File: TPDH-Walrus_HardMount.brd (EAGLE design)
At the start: 16 x 40 mm, 37 parts, among them Q2 DMG3404, U1 MS5803-14BA, U2 SN65HVD33RHL, U4 MCP3421A3, U5 TPS79733, U6 MAX6070AAUT18, U7 TXS0102DQM

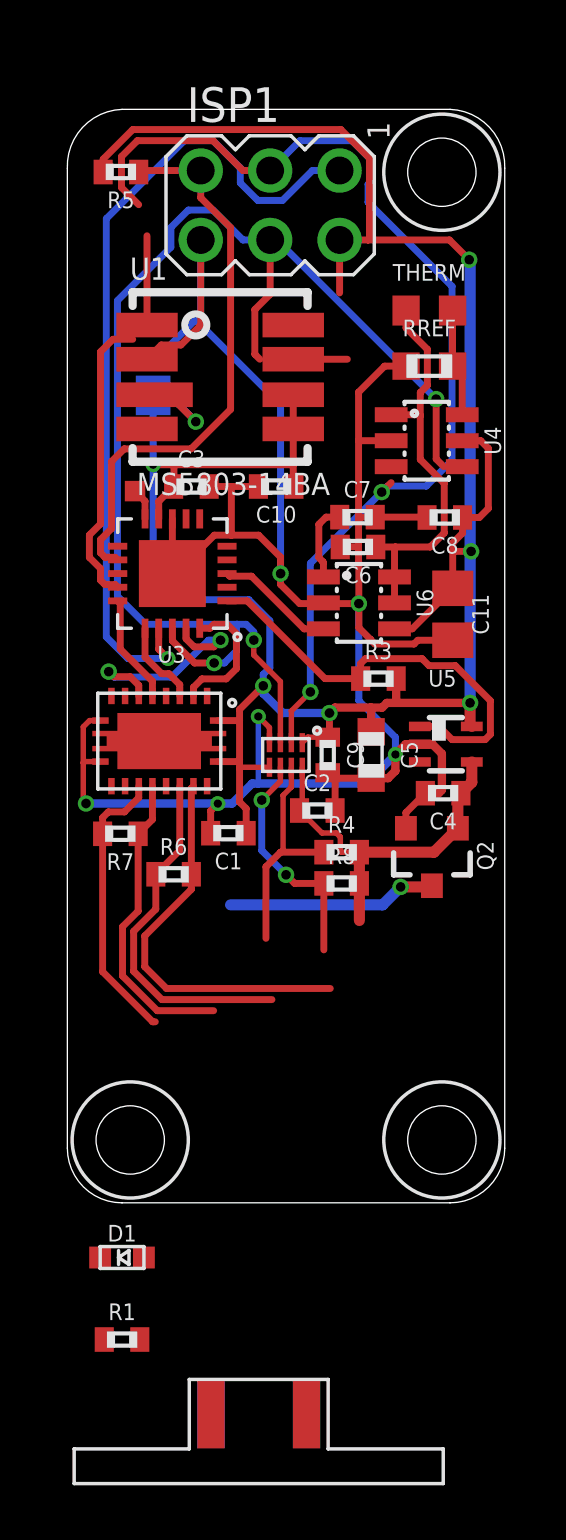
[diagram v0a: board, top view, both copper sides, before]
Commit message: Initial layout for Hard mount (v0.1) variant, cleanup required
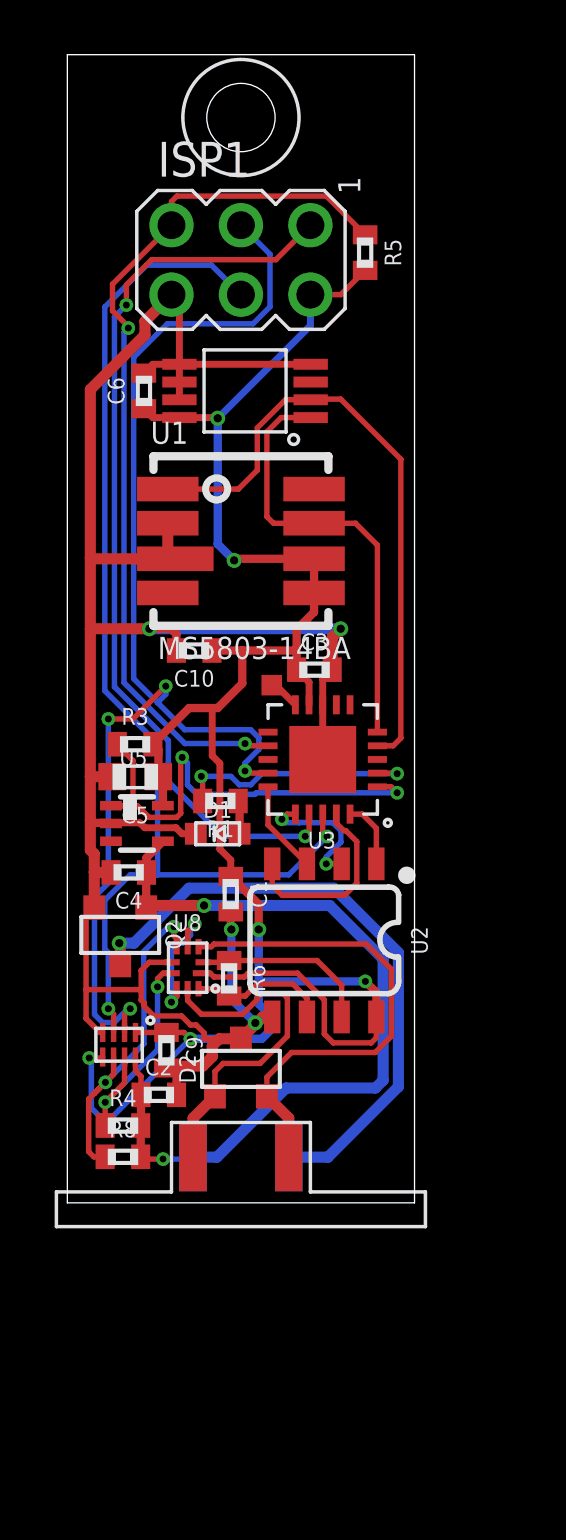
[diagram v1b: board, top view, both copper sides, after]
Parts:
- removed C11: 10uF, bschulz:C0805
- removed C7, C8: 0.1uF, bschulz_passives:C0402
- removed H2, H3: (no value), bschulz:2_56
- removed JP1: JUMPER-SMT_3_1-NC_PASTE_SILK, SparkFun-Jumpers:SMT-JUMPER_3_1-NC_PASTE_SILK
- removed R7: (no value), bschulz_passives:R0402
- removed RREF: 10k, bschulz_passives:R0603
- removed THERM: 10k, bschulz:R0603
- removed U6: MAX6070AAUT18, bschulz:SOT23-6L
- added D2: (no value), bschulz:SOT23-3
- added U8: NS5A4684S, bschulz:WQFN10
- C6: value 0.1uF -> (none)
- U2: value SN65HVD33RHL -> SN65HVD72DSOIC; device bschulz:VQFN-20_POWER -> bschulz:SO08
- U4: value MCP3421A3 -> MCP9808DFNMSOP; device bschulz:SOT23-6L -> bschulz:MSOP_8
- moved R1 20.0 mm to (5.60, 14.7), turned to 180 degrees
- moved D1 15.9 mm to (5.50, 13.5)
- moved R4 12.8 mm to (2.03, 2.83)
- moved R8 12.8 mm to (2.03, 1.68)
- moved C9 12.3 mm to (3.62, 5.58)
- moved U7 12.2 mm to (1.89, 5.78)
- moved C2 11.9 mm to (3.34, 3.95)
- moved C4 11.9 mm to (2.25, 12.1)
- moved Q2 11.8 mm to (1.94, 9.80)
- moved U5 11.7 mm to (2.55, 13.9)
- moved C6 9.69 mm to (2.80, 29.7), turned to 90 degrees
- moved U2 9.47 mm to (9.40, 9.60), turned to 180 degrees
- moved U$1 9.42 mm to (6.35, 0.40)
- moved R5 9.41 mm to (10.9, 34.8), turned to 270 degrees
- moved R3 9.22 mm to (2.48, 16.8)
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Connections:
- removed net N$11: C7.1, U6.1
- removed net SPI-I2C-SWITCH: JP1.2, U1.3
- removed net VREF: C6.1, THERM.1, U4.1, U6.5, U6.6
- removed net VTHERM-: RREF.2, THERM.2, U4.6
- new net OUTPUT_SEL: U8.4, U8.8
- new net TEMP_ALERT: U4.3
- net +3V3: now also C6.1, U2.8, U4.8, U8.1; no longer C11.1, C8.1, JP1.1, U2.1, U2.20, U4.5, U6.4
- net A: now also U2.6, U8.10; no longer R7.2, U2.14, U2.18
- net B: now also U2.7, U8.2; no longer R7.1, U2.15, U2.17
- net GND: now also D2.3, U1.3, U2.5, U4.4, U4.5, U4.6, U4.7, U8.6; no longer C11.2, C7.2, C8.2, JP1.3, RREF.1, U2.10, U2.11, U4.2, U6.2
- net REF_EN: no longer U6.3
- net RX: now also U2.1; no longer U2.3
- net SCL_HV: now also U8.7
- net SCL_OB: now also U4.2; no longer U4.3
- net SDA_HV: now also U8.5
- net SDA_OB: now also U4.1; no longer U4.4
- net SIG1: now also D2.1, U8.9
- net SIG2: now also D2.2, U8.3
- net SN_DE: now also U2.3; no longer U2.6
- net SN_RE: now also U2.2; no longer U2.4
- net TX: now also U2.4; no longer U2.7
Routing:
- net A: track 24.8 -> 5.16 mm
- net SCL_OB: track 3.27 -> 22.9 mm
- net SIG2: track 0.00 -> 18.4 mm
- net +3V3: track 94.0 -> 76.1 mm
- net B: track 24.2 -> 6.63 mm
- net VIN+: track 13.9 -> 30.5 mm, vias 0 -> 2
- net VIN-: track 7.65 -> 22.8 mm
- net VREF: track 14.8 -> 0.00 mm
- net SDA_OB: track 1.98 -> 16.2 mm
- net SIG1: track 0.00 -> 12.8 mm
- net /RESET: track 20.9 -> 32.8 mm, vias 0 -> 2
- net STAT_LED: track 0.00 -> 9.11 mm, vias 0 -> 2
- net GND: track 92.6 -> 84.0 mm, vias 6 -> 4
- net SDA: track 48.7 -> 42.6 mm, vias 3 -> 2
- net OUTPUT_SEL: track 0.00 -> 4.87 mm, vias 0 -> 2
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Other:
- board size 16 x 40 mm -> 12.7 x 42 mm
- board text removed: "I2C <3 m"
- board text removed: "Rx+"
- board text removed: "Rx-"
- board text removed: "SCL"
- board text removed: "SDA"
- board text removed: "Tx+"
- board text removed: "Tx-"
- board text removed: "V+"
- board text removed: "V-"

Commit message: Continued layout, final cleanup required
Cleanup and pours required
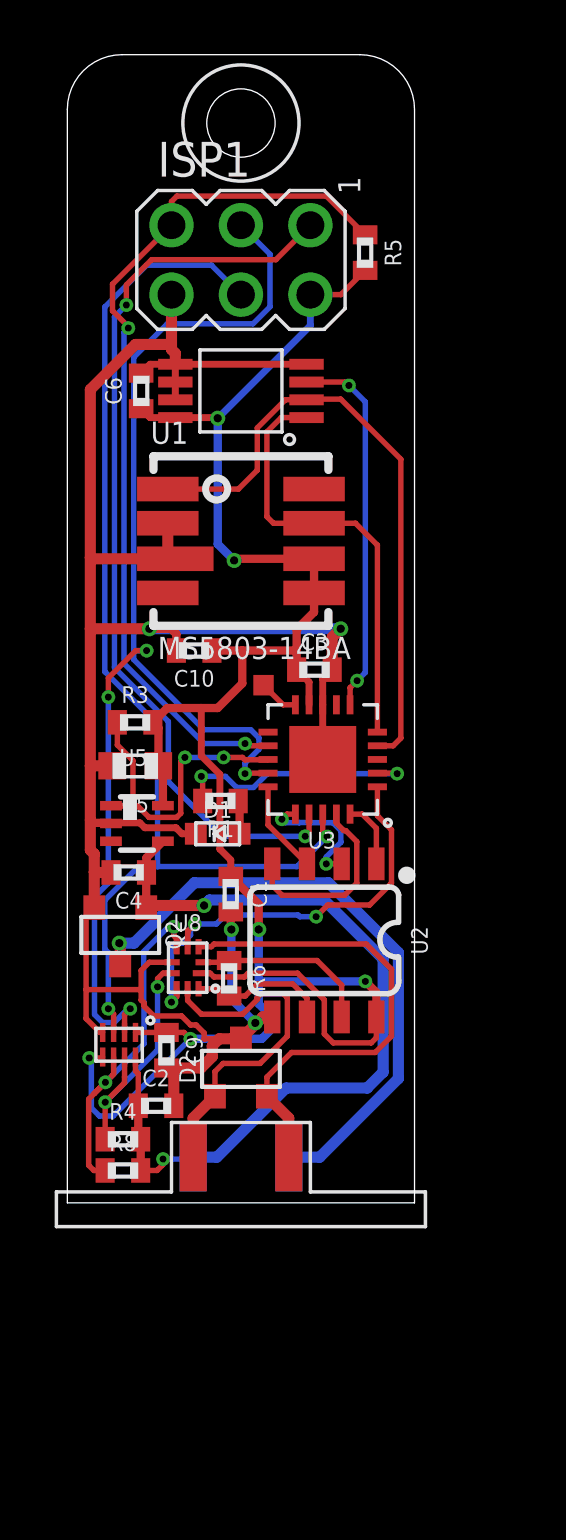
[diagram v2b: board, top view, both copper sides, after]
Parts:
- moved R3 0.80 mm to (2.48, 17.6)
- moved R4 0.50 mm to (2.03, 2.33)
- moved R8 0.50 mm to (2.03, 1.18)
- moved C2 0.41 mm to (3.24, 3.55)
- moved C5 0.40 mm to (2.48, 16.0)
- moved U$12 0.30 mm to (7.18, 18.9)
- moved H1 0.20 mm to (6.35, 39.5)
- moved U4 0.15 mm to (6.35, 29.7)
- moved C6 0.10 mm to (2.70, 29.7)
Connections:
- removed net N$1: U3.7
- removed net N$3: U3.6
- net OUTPUT_SEL: now also U3.1
- net PG: now also U3.13; no longer U3.1
- net TEMP_ALERT: now also U3.6
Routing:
- net TEMP_ALERT: track 0.00 -> 13.8 mm, vias 0 -> 2
- net OUTPUT_SEL: track 4.87 -> 16.5 mm, vias 2 -> 3
- net PG: track 17.6 -> 11.8 mm
- net VIN+: track 30.5 -> 31.2 mm
- net +3V3: track 76.1 -> 76.8 mm
- net SDA_HV: track 12.7 -> 13.2 mm
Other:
- outline, holes or cut-outs redrawn

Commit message: Minor layout updates, sent to fab
Cleaned up layout, sent to fab
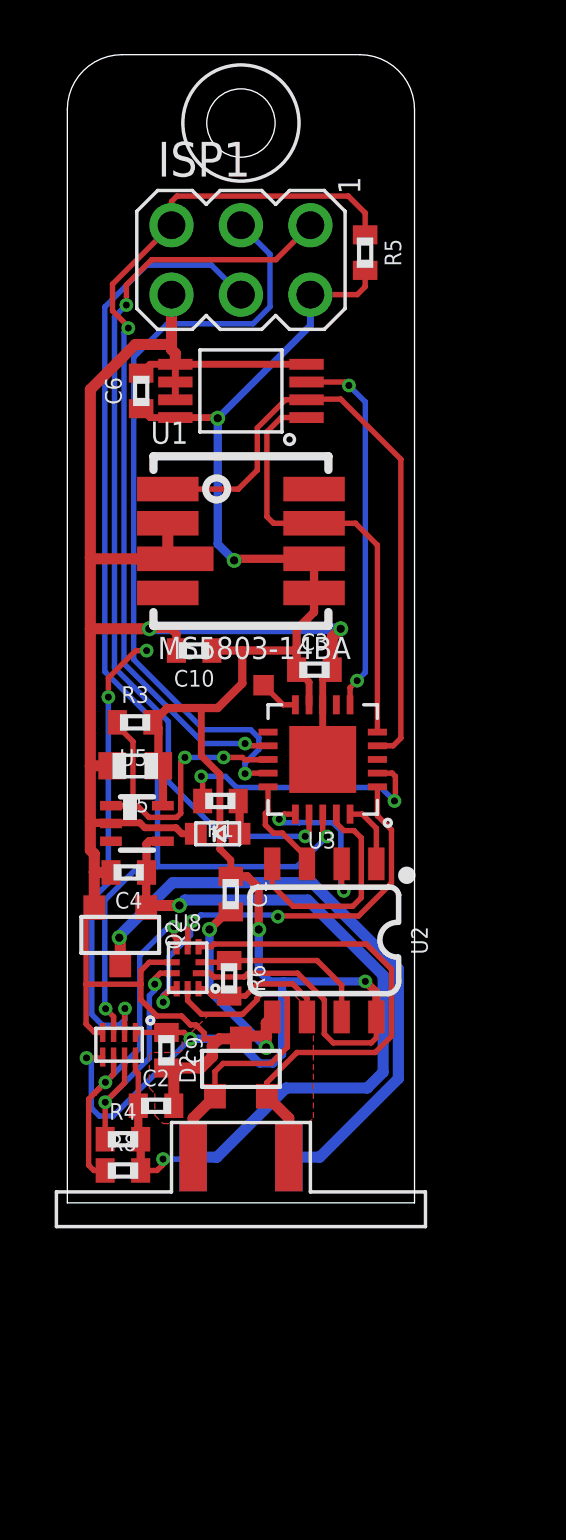
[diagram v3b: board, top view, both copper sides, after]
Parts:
- U4: value MCP9808DFNMSOP -> MCP9808MSOP
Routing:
- net +3V3: track 76.8 -> 78.9 mm
- net GND: track 83.6 -> 85.3 mm
- net SN_RE: track 4.90 -> 6.37 mm
- net TX: track 7.09 -> 8.14 mm
- net STAT_LED: track 9.19 -> 9.98 mm
- added copper zone on layer 1, net GND
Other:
- board text added: "Project-TPDH-Walrus v0.1.0 07-15-2019 Based on TP-Downhole by Schulz, Sandell, Wickert A. Wickert Northern Widget LLC and University of Minnesota"
- board text removed: "0x76"
- board text removed: "0x77"
- board text removed: "ALT"
- board text removed: "DEFAULT"
- board text removed: "Project-TPDH-Walrus v0.0.0 02-26-2018 Based on TP-Downhole by Schulz, Sandell, Wickert A. Wickert Northern Widget LLC and University of Minnesota"
- board text removed: "RS485: <1000 m"

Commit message: Added BOM for hard mount, minor part number cleanup
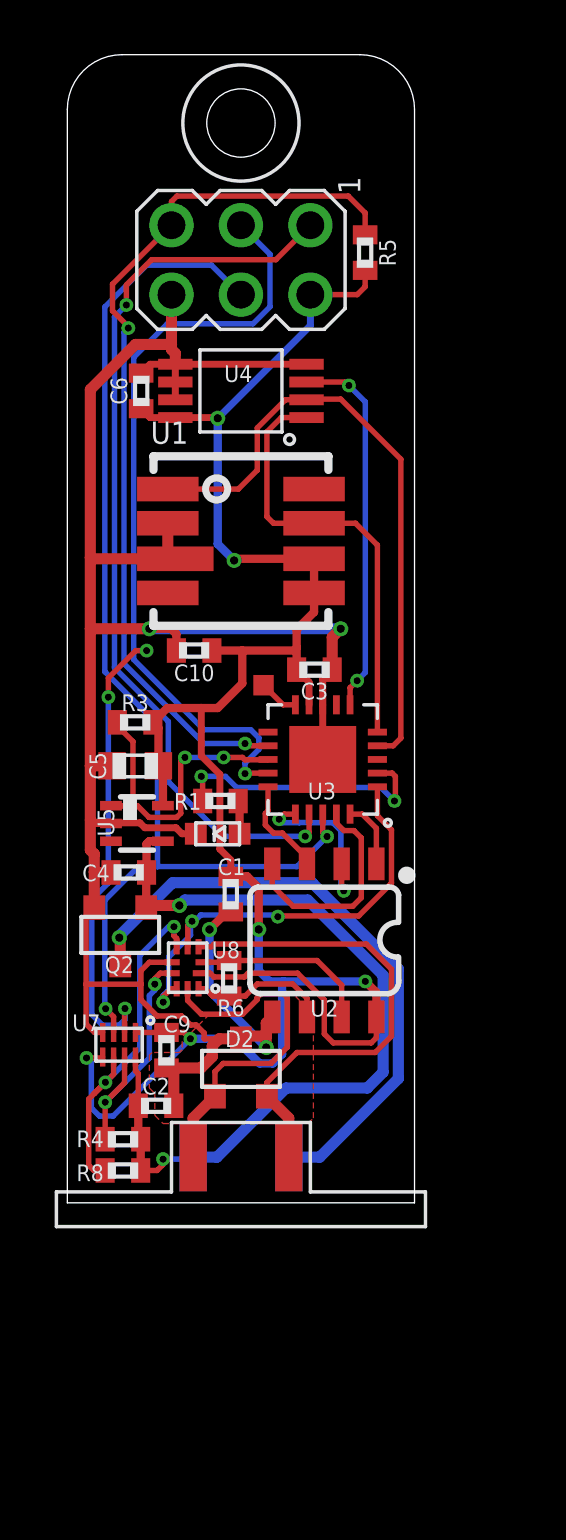
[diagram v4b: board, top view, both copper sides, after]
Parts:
- C6: value (none) -> 0.1uF
- R1: value (none) -> 1k
- R6: value (none) -> 100

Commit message: Update to v0.1 hardware, review required
Initial update complete, requires review and verification of various fixes
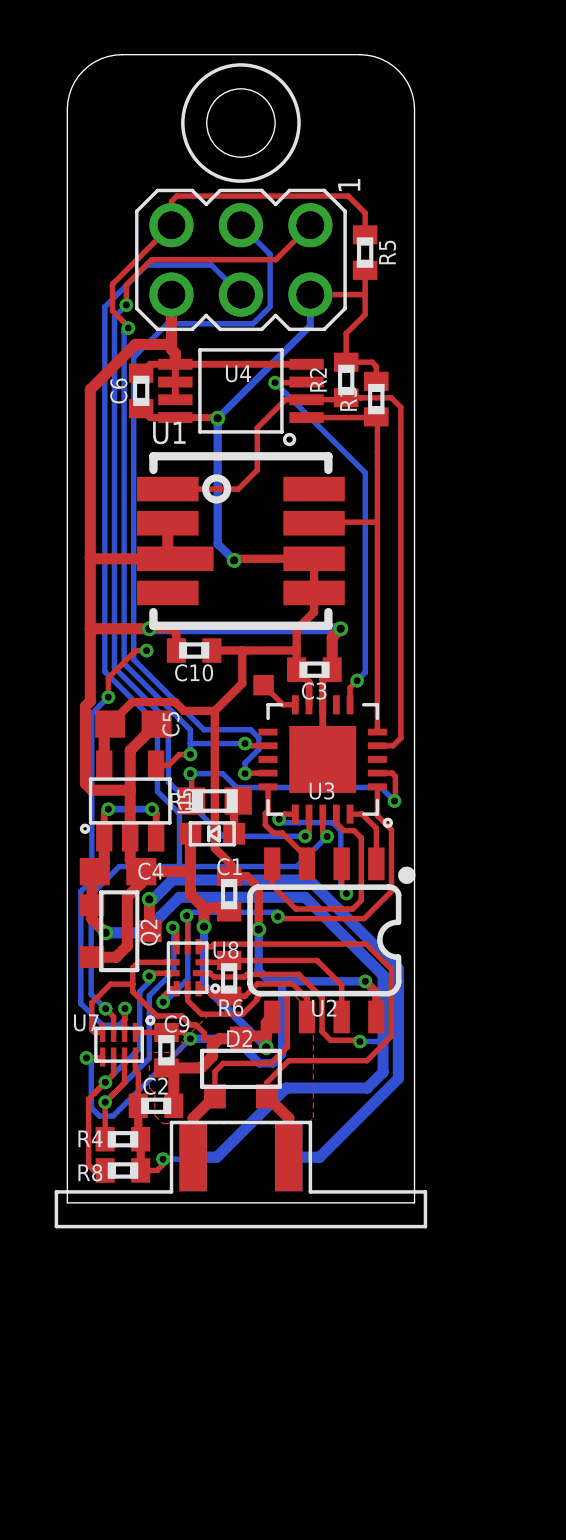
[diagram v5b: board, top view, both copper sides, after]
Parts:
- added R2: 10k, bschulz_passives:R0402
- C4: value 0.1uF -> 1uF; device bschulz_passives:C0402 -> bschulz:C0603
- C5: device bschulz_passives:C0603 -> bschulz:C0603
- R1: device bschulz_passives:R0402 -> bschulz_passives:R0603
- U5: value TPS79733 -> LP39883.3VDBV; device bschulz:DCK_R-PDSO-G5 -> bschulz:DBV0005A
- moved R3 14.8 mm to (11.3, 29.4), turned to 90 degrees
- moved C5 1.53 mm to (2.42, 17.5), turned to 0 degrees
- moved U5 0.86 mm to (2.30, 14.7), turned to 90 degrees
- moved C4 0.39 mm to (1.85, 12.1), turned to 0 degrees
- moved D1 0.20 mm to (5.30, 13.5)
- moved R1 0.20 mm to (5.40, 14.7)
- moved Q2 0.14 mm to (1.90, 9.94), turned to 270 degrees
- moved C1 0.06 mm to (5.92, 11.3)
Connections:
- removed net /RESET: ISP1.5, R5.1, U3.12
- new net !RESET: ISP1.5, R5.1, U3.12, U5.4
- net +3V3: now also R2.2; no longer U8.1
- net PG: no longer R3.1, U5.1
- net SCL_HV: now also U8.5; no longer U8.7
- net SCL_OB: now also R2.1
- net SDA_HV: now also U8.7; no longer U8.5
- net SDA_OB: now also R3.1
- net VIN+: now also U5.1, U5.3, U8.1; no longer U5.4
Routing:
- net !RESET: track 0.00 -> 34.9 mm, vias 0 -> 3
- net /RESET: track 32.8 -> 0.00 mm, vias 2 -> 0
- net VIN+: track 31.1 -> 46.3 mm, vias 2 -> 5
- net PG: track 11.8 -> 0.02 mm, vias 2 -> 0
- net +3V3: track 78.9 -> 74.7 mm
- net GND: track 85.3 -> 89.6 mm
- net SCL_HV: track 9.29 -> 11.5 mm
- net SDA_HV: track 13.2 -> 11.0 mm
- net VIN-: track 22.6 -> 21.1 mm
- net SCL_OB: track 23.2 -> 24.4 mm
- net SDA: track 42.3 -> 43.4 mm
- net OUTPUT_SEL: track 16.9 -> 17.7 mm
- net TEMP_ALERT: track 13.8 -> 14.5 mm
- net STAT_LED: track 9.98 -> 10.5 mm

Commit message: Board cleanup, final DFM for v0.2, added gerbers
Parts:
- moved R1 0.30 mm to (5.40, 15.0)
- moved R5 0.27 mm to (10.9, 34.5)
- moved C1 0.10 mm to (5.92, 11.4)
- moved R6 0.10 mm to (5.92, 8.31)
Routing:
- net SCL: track 46.3 -> 45.3 mm
- net +3V3: track 74.7 -> 73.8 mm
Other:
- board text added: "Project-TPDH-Walrus v0.2.0 07-15-2019 Based on TP-Downhole by Schulz, Sandell, Wickert A. Wickert Northern Widget LLC and University of Minnesota"
- board text removed: "Project-TPDH-Walrus v0.1.0 07-15-2019 Based on TP-Downhole by Schulz, Sandell, Wickert A. Wickert Northern Widget LLC and University of Minnesota"
